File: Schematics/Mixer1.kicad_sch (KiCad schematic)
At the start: 47 parts, among them J53 Conn_01x02, J54 Conn_01x02, J55 Conn_01x02, J56 Conn_01x02, J57 Conn_01x02, J58 Conn_01x02, J59 Conn_01x02, J60 Conn_01x02, J61 Conn_01x03, J62 AudioJack2_Ground, J63 Conn_01x02, U104 TL084, U105 TL084, U106 LM358, U86 LM358

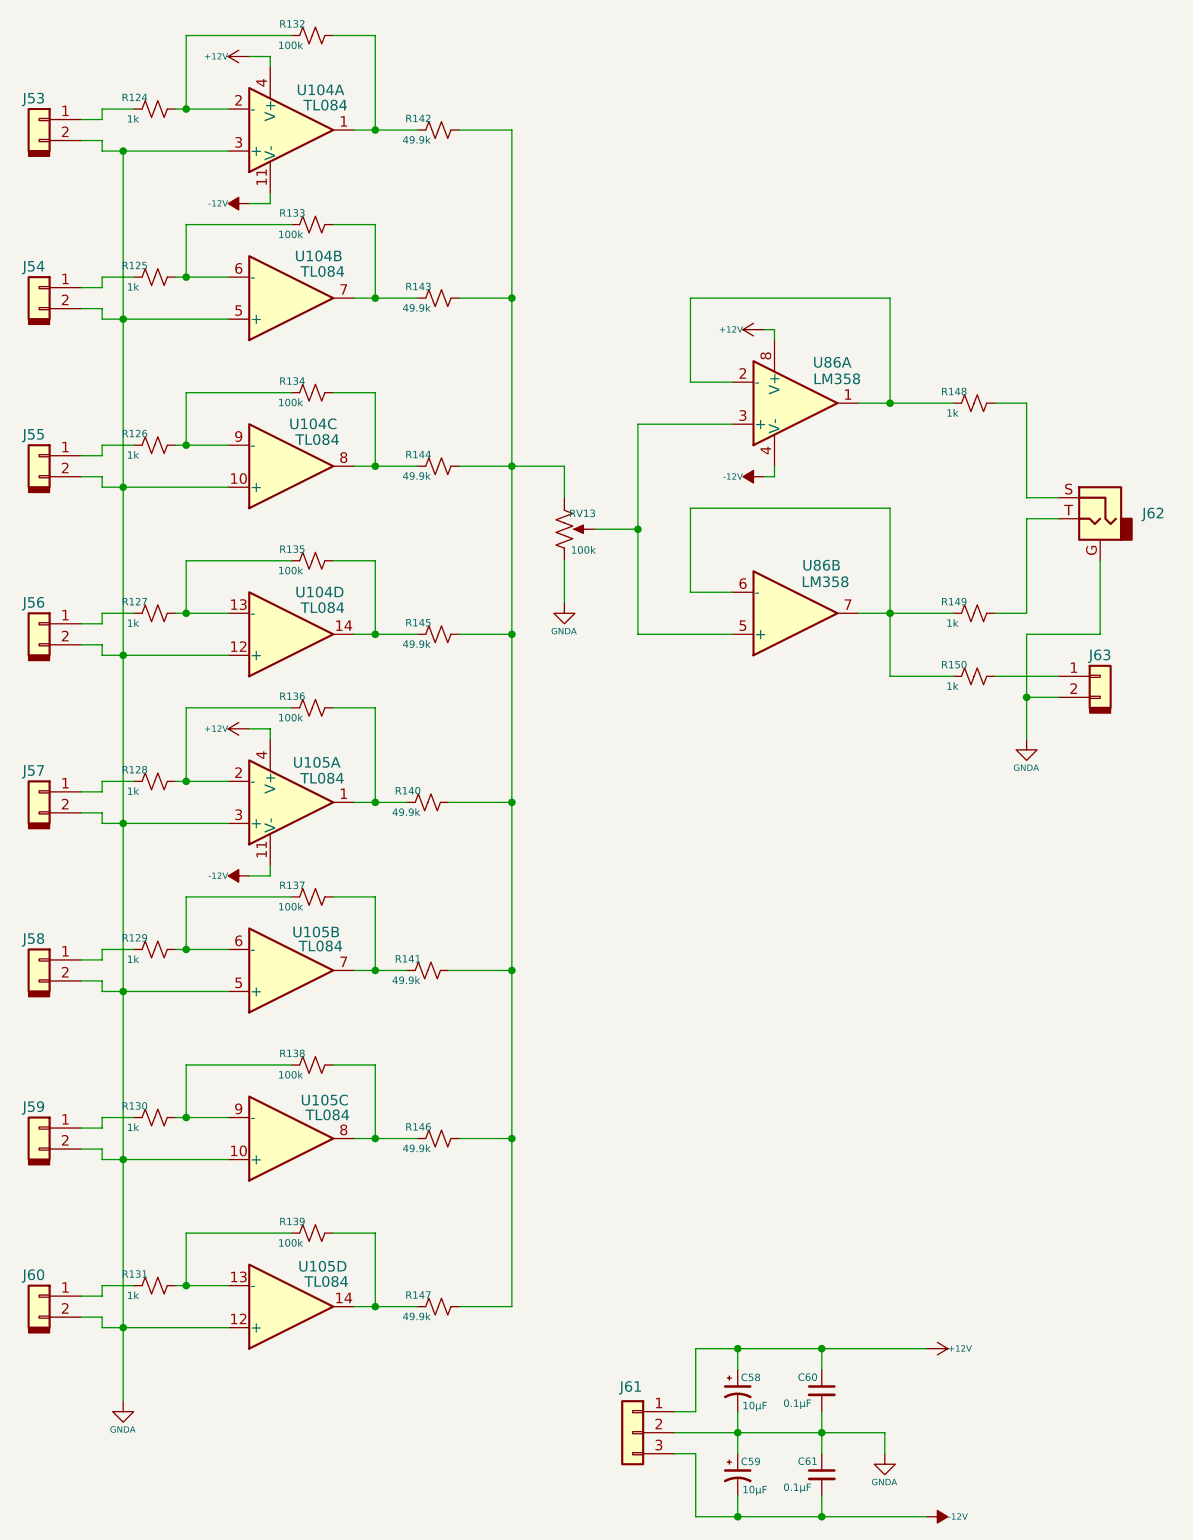
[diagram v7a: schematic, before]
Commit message: Partial software with complete hardware on best 3 state filter with 4 outputs.
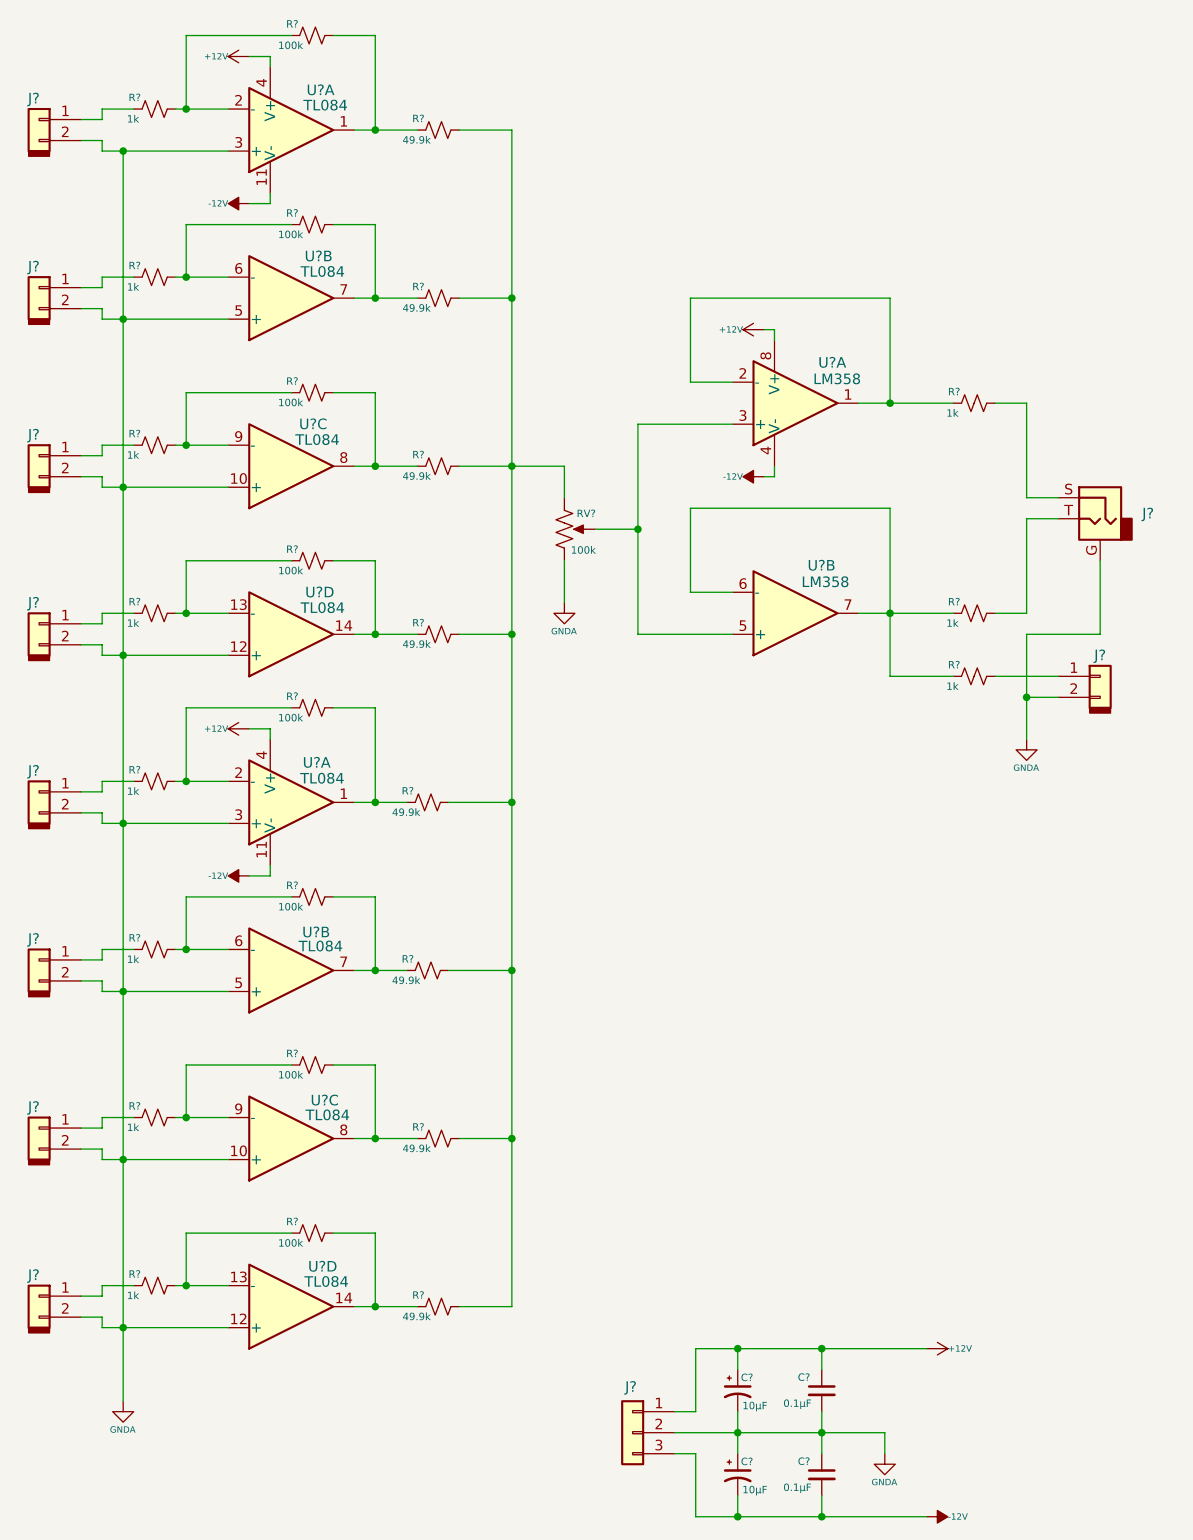
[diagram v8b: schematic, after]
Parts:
- renumbered C61 to C?, C60 to C?, C59 to C?, C58 to C?, J59 to J?, J63 to J?, J57 to J?, J55 to J?, J62 to J?, J58 to J?, J53 to J?, J61 to J?, J54 to J?, J56 to J?, J60 to J?, R149 to R?, R143 to R?, R136 to R?, R135 to R?, R131 to R?, R138 to R?, R146 to R?, R144 to R?, R128 to R?, R140 to R?, R145 to R?, R132 to R?, R125 to R?, R150 to R?, R139 to R?, R141 to R?, R130 to R?, R142 to R?, R127 to R?, R126 to R?, R129 to R?, R148 to R?, R133 to R?, R147 to R?, R137 to R?, R124 to R?, R134 to R?, RV13 to RV?, U104 to U?, U105 to U?, U106 to U?, U86 to U?
